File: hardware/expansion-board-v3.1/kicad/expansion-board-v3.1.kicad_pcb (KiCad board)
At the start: 6 copper layers, 100 x 62 mm, 156 parts, among them J1 PinHeader_2x20_P2.54mm_Vertic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, J2 U.FL_Hirose_U.FL-R-SMT-1_Vert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, J4 USB_C_Receptacle_HRO_TYPE-C-3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, J5 U.FL_Hirose_U.FL-R-SMT-1_Vert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, J6 U.FL_Hirose_U.FL-R-SMT-1_Vert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, J8 U.FL_Hirose_U.FL-R-SMT-1_Vert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, Q2 SOT-23, Q3 SOT-23, Q4 SOT-23, Q5 SOT-23, SW1 SolderJumper-2_P1.3mm_Open_Pa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, SW2 SolderJumper-2_P1.3mm_Open_Pa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, U1 SOT-23-5, U10 QFN-48-1EP_7x7mm_P0.5mm_EP5.1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, U11 DFN-8-1EP_2x2mm_P0.5mm_EP0.86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, U12 SOT-363_SC-70-6, U13 AD8319_LFCSP-8-EP, U14 MSOP-8_3x3mm_P0.65mm, U15 SOT-23-6, U16 SOT-363_SC-70-6, U17 SOT-363_SC-70-6, U2 SOT-23-5, U3 SOT-23-5, U4 BNO085_LGA-28, U5 BMP388_LGA-10, U6 LGA-16_3x3mm_P0.5mm, U7 ATGM336H_LCC-18, U8 QFN-56-1EP_7x7mm_P0.4mm_EP3.2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, U9 SOIC-8_5.3x5.3mm_P1.27mm, Y1 Crystal_SMD_3225-4Pin_3.2x2.5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, Y2 Crystal_SMD_3225-4Pin_3.2x2.5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, Y3 Crystal_SMD_3215-2Pin_3.2x1.5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

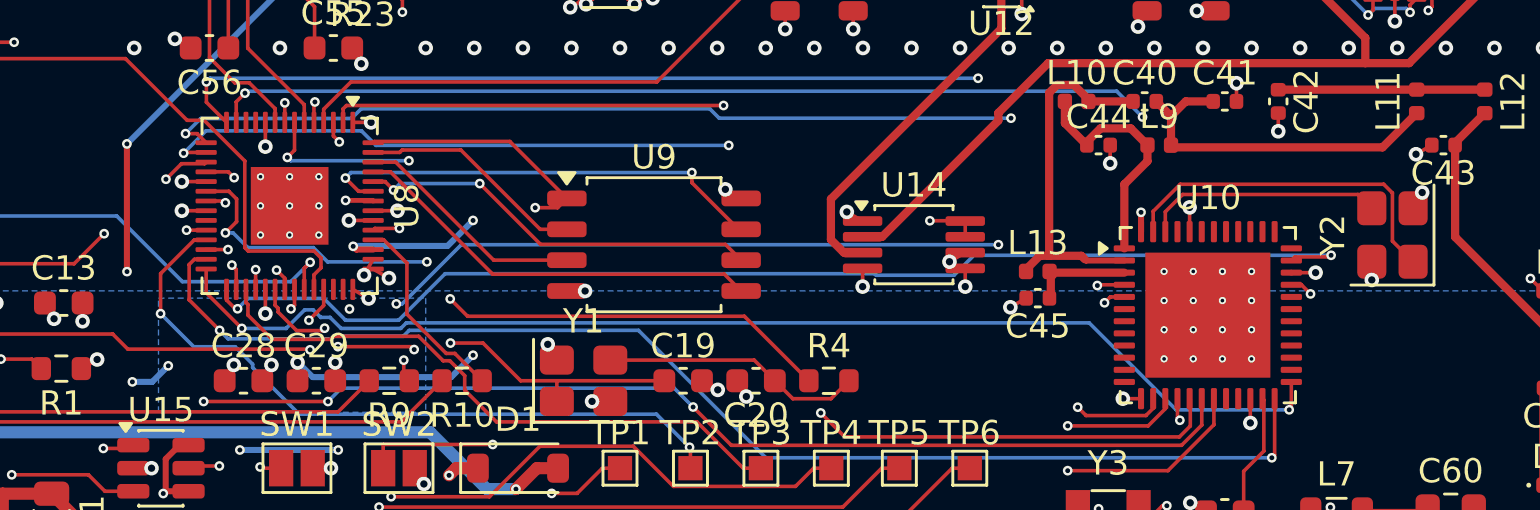
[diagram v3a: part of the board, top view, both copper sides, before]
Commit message: feat(hw): 未连通归零 —— 手工让开两个过孔，两条死线一次布通
    真缺线 0 / 孤立断头铜 0 / 焊盘未接覆铜 0 / 铜层 DRC 0 违例
    射频 160 段全 F.Cu、0 过孔，In1 参考面完整

全项归零，这是 v3.1 第一次。

## 怎么破的

卡了很久的 SUBG_VDDR(U10.45) 和 RP_1V1(U8.23)，我试过 via_keepout 三种形态、
预扇出环、ripup 让路，都不赚（数据在下面）。**评审直接在 KiCad 里把挡路的两个
过孔往外挪了**：

    U8   3V3_DIG 孔  (83.96,80.70)  → (83.35,80.30)
    U8   SWCLK   孔  (84.16,81.50)  → (83.63,82.03)
    U10  3V3_DIG 孔  (125.45,80.56) → (126.58,80.43)

让出通道后他把两条线拉了出来（还顺手在 In2 布通了 SUBG_IRQ 4 段），
剩两个线头交给 route_fix，**一次布通，0 失败**。

## 他先前的两个判断都被数据证实了

**判断一："多个针脚过孔要留下足够空间"** —— 是硬规则，且能算出确切数字：

    通道净空 ≥ 线宽 + 2×净空     信号 0.15+0.30=0.45mm ／ 电源 0.25+0.30=0.55mm

出事的两处正好卡在线下面：U8 两孔之间只有 0.425mm（差 0.125），
U10 pin45 到 3V3_DIG 孔 0.45mm（差 0.10）。差的就是这一点点。

**判断二："先过孔还是先走线"** —— freerouting 是边布线边打孔，先布的线把后面
的孔位堵死。仓里 fanout_ring.py 正是为此写的（文件头："在 freerouting 之前占住
引脚净空环"），但从没进过流程。

## 顺带修掉的、以及试过不赚的

- **route_rf 的缝合过孔写死 0.6/0.3**，而板规是 0.4/0.2。这类孔有 **242 个，
  占全板 451 个过孔的 54%** —— 一大半过孔都胖了 0.1mm 半径。挡住 U8.23 的正是
  其中一个。改到板规后同一对孔的净空 0.325 → 0.425mm。
  **同族问题（改了尺寸，写死的副本没跟着改）这是第 5 次**，前四次见
  memory/project_hardcoded_dimension_copies.md。fanout_v31.py 和 stitch.py 里
  还各有一处，这两个脚本不在流程里，留待启用时修。
- **fanout_ring 排号用错索引**：`row = i % stride` 的 i 是 todo 的序号，而 todo
  滤掉了 GND/RF 引脚，于是和物理位置脱钩——两个只隔 0.4mm 的引脚可能拿到同一排。
  改用该边全部引脚的排序序号。另加 PK_WHY=<ref.pin> 诊断，打印每个候选位被谁挡住。
- **0.4mm pitch 下每脚都扇出物理上不成立**：孔半径 0.2 + stub 半宽 0.075 +
  净空 0.2 = 0.475mm > 引脚间距 0.4mm。所以 72 脚里 25 个"无位"是正常结果。

试过、不赚、已回退的（同一布局，收敛后未连通）：

    什么都不加            2   ← 当时最好
    via_keepout 实心矩形  7   ← 连芯片下方可用区和路过走线的换层都封死
    via_keepout 口字环    3
    预扇出环(先放孔)      5   ← 原理对，但一口气放 47 个孔把空间挤没了
    手工挪 3 个孔     0   ← 精准，代价为零

教训：**这类局部死结，人挪三个孔胜过我改五版算法**。自动化该做的是把规则固化下来
（净空式子、先放孔的顺序、尺寸同步），而不是替代这三下。

## ⚠️ 一个已知风险，下一步必须处理

`gen_pcb.py:194` 是 `pcbnew.NewBoard()` —— **跑 run_route.sh 会从零重建板子，
评审这次手工挪的孔和拉的线全部丢失**。PLACEMENT.py 只固化元件位置，走线没有任何
持久化，而且现在也无法事后识别（全板 IsLocked 都是 False，手画的和 freerouting
布的混在一起）。所以**在补上固化机制之前，不要再跑整条链**。
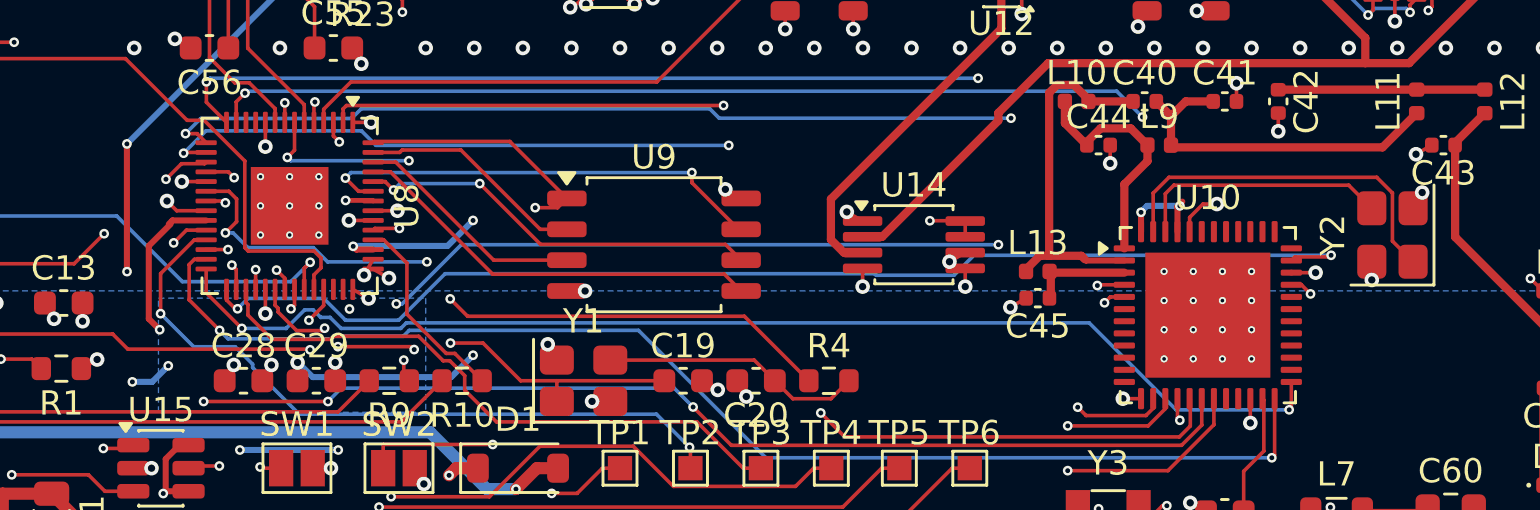
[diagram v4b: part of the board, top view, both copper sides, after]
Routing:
- net RP_1V1: track 39.2 -> 45.7 mm, vias 9 -> 10
- net SUBG_VDDR: track 31.6 -> 34.7 mm, vias 2 -> 3
- net 3V3_DIG: track 36.8 -> 38.5 mm
- net SWCLK: track 41.4 -> 42.9 mm
- net SUBG_X48N: track 9.85 -> 10.6 mm
- net SUBG_X48P: track 14.5 -> 15.2 mm
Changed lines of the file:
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@@
 	)
 	(segment
+		(start 125.45 80.975)
+		(end 125.45 81.5625)
+		(width 0.15)
+		(layer "F.Cu")
+		(net "3V3_DIG")
+	)
+	(segment
 		(start 127.95 88.4375)
 		(end 127.95 89.4375)
@@
 	)
 	(segment
-		(start 63.95 75.975)
-		(end 63.95 76.975)
+		(start 84.9625 80.7)
+		(end 83.75 80.7)
 		(width 0.15)
 		(layer "F.Cu")
@@
 	)
 	(segment
-		(start 84.9625 80.7)
-		(end 83.9625 80.7)
+		(start 63.95 75.975)
+		(end 63.95 76.975)
 		(width 0.15)
 		(layer "F.Cu")
@@
 	)
 	(segment
+		(start 126 80.425)
+		(end 125.45 80.975)
+		(width 0.15)
+		(layer "F.Cu")
+		(net "3V3_DIG")
+	)
+	(segment
 		(start 128.225 97)
 		(end 128.6 96.3505)
@@
 	)
 	(segment
+		(start 126.575 80.425)
+		(end 126 80.425)
+		(width 0.15)
+		(layer "F.Cu")
+		(net "3V3_DIG")
+	)
+	(segment
 		(start 70.225 98.3)
 		(end 69.5755 97.925)
@@
 	)
 	(segment
-		(start 125.45 81.5625)
-		(end 125.45 80.5625)
+		(start 83.75 80.7)
+		(end 83.35 80.3)
 		(width 0.15)
 		(layer "F.Cu")
@@
 	)
 	(via
-		(at 125.45 80.5625)
+		(at 126.575 80.425)
 		(size 0.6)
 		(drill 0.3)
@@
 	)
 	(via
-		(at 83.9625 80.7)
+		(at 83.35 80.3)
 		(size 0.6)
 		(drill 0.3)
@@
 	)
 	(segment
+		(start 124.95 80.525)
+		(end 125.15 80.325)
+		(width 0.25)
+		(layer "F.Cu")
+		(net "SUBG_VDDR")
+	)
+	(segment
 		(start 125.5296 95.7954)
 		(end 124.1228 94.3886)
@@
 	)
 	(segment
+		(start 124.95 81.5625)
+		(end 124.95 80.525)
+		(width 0.25)
+		(layer "F.Cu")
+		(net "SUBG_VDDR")
+	)
+	(segment
 		(start 126.8166 94.5084)
 		(end 131.1541 94.5084)
@@
 		(net "SUBG_VDDR")
 	)
+	(via
+		(at 125.05 80.5)
+		(size 0.4)
+		(drill 0.2)
+		(layers "F.Cu" "B.Cu")
+		(net "SUBG_VDDR")
+	)
+	(segment
+		(start 123.4 80.8)
+		(end 123.7 80.5)
+		(width 0.25)
+		(layer "B.Cu")
+		(net "SUBG_VDDR")
+	)
+	(segment
+		(start 123.7 80.5)
+		(end 125.05 80.5)
+		(width 0.25)
+		(layer "B.Cu")
+		(net "SUBG_VDDR")
+	)
 	(segment
 		(start 123.45 80.7643)
@@
 	)
 	(segment
-		(start 84.8572 82.8758)
-		(end 83.3085 81.3271)
+		(start 84.8572 88.5543)
+		(end 84.8572 83.9572)
 		(width 0.15)
 		(layer "In2.Cu")
@@
 	)
 	(segment
-		(start 83.3085 81.3271)
-		(end 83.3085 79.404)
+		(start 84.8572 83.9572)
+		(end 82.725 81.825)
 		(width 0.15)
 		(layer "In2.Cu")
@@
 	)
 	(segment
-		(start 84.8572 88.5543)
-		(end 84.8572 82.8758)
+		(start 82.725 81.825)
+		(end 82.725 79.9875)
+		(width 0.15)
+		(layer "In2.Cu")
+		(net "SUBG_IRQ")
+	)
+	(segment
+		(start 82.725 79.9875)
+		(end 83.3085 79.404)
 		(width 0.15)
 		(layer "In2.Cu")
@@
 	)
 	(segment
-		(start 124.45 81.5625)
-		(end 124.45 80.744)
+		(start 132 79.65)
+		(end 132.95 80.6)
 		(width 0.15)
 		(layer "F.Cu")
@@
 	)
 	(segment
-		(start 124.45 80.744)
-		(end 125.163 80.031)
+		(start 124.45 81.5625)
+		(end 124.45 80)
 		(width 0.15)
 		(layer "F.Cu")
@@
 	)
 	(segment
-		(start 125.163 80.031)
-		(end 132.381 80.031)
+		(start 124.8 79.65)
+		(end 132 79.65)
 		(width 0.15)
 		(layer "F.Cu")
@@
 	)
 	(segment
-		(start 132.381 80.031)
-		(end 132.95 80.6)
+		(start 124.45 80)
+		(end 124.8 79.65)
 		(width 0.15)
 		(layer "F.Cu")
@@
 	)
 	(segment
-		(start 133.8 79.97)
-		(end 133.8 81.95)
+		(start 124.6 79.325)
+		(end 133.155 79.325)
 		(width 0.15)
 		(layer "F.Cu")
@@
 	)
 	(segment
-		(start 125.0652 79.6108)
-		(end 133.4408 79.6108)
+		(start 133.8 81.95)
+		(end 134.65 82.8)
 		(width 0.15)
 		(layer "F.Cu")
@@
 	)
 	(segment
-		(start 133.8 81.95)
-		(end 134.65 82.8)
+		(start 123.95 81.5625)
+		(end 123.95 79.975)
 		(width 0.15)
 		(layer "F.Cu")
@@
 	)
 	(segment
-		(start 123.95 80.726)
-		(end 125.0652 79.6108)
+		(start 133.155 79.325)
+		(end 133.8 79.97)
 		(width 0.15)
 		(layer "F.Cu")
@@
 	)
 	(segment
-		(start 123.95 81.5625)
-		(end 123.95 80.726)
+		(start 133.8 79.97)
+		(end 133.8 81.95)
 		(width 0.15)
 		(layer "F.Cu")
@@
 	)
 	(segment
-		(start 133.4408 79.6108)
-		(end 133.8 79.97)
+		(start 123.95 79.975)
+		(end 124.6 79.325)
 		(width 0.15)
 		(layer "F.Cu")
@@
 	)
 	(segment
+		(start 82.6 85.15)
+		(end 83.05 85.6)
+		(width 0.25)
+		(layer "F.Cu")
+		(net "RP_1V1")
+	)
+	(segment
 		(start 91.8129 80.2754)
 		(end 91.8375 80.3)
@@
 	)
 	(segment
+		(start 82.6 82.15)
+		(end 82.6 85.15)
+		(width 0.25)
+		(layer "F.Cu")
+		(net "RP_1V1")
+	)
+	(segment
 		(start 85.725 87.7)
 		(end 86.1 87.0505)
@@
 	)
 	(segment
+		(start 84.9625 81.1)
+		(end 83.575 81.1)
+		(width 0.25)
+		(layer "F.Cu")
+		(net "RP_1V1")
+	)
+	(segment
 		(start 91.1493 82.3)
 		(end 91.0149 82.1656)
@@
 	)
 	(segment
+		(start 83.5 81.25)
+		(end 82.6 82.15)
+		(width 0.25)
+		(layer "F.Cu")
+		(net "RP_1V1")
+	)
+	(segment
+		(start 83.575 81.1)
+		(end 83.425 81.25)
+		(width 0.25)
+		(layer "F.Cu")
+		(net "RP_1V1")
+	)
+	(segment
 		(start 90.7031 80.2754)
 		(end 91.8129 80.2754)
@@
 	)
 	(via
+		(at 83.05 85.6)
+		(size 0.4)
+		(drill 0.2)
+		(layers "F.Cu" "B.Cu")
+		(net "RP_1V1")
+	)
+	(via
 		(at 90.4 90.55)
 		(size 0.4)
@@
 	)
 	(segment
-		(start 84.9625 81.5)
-		(end 84.155 81.5)
+		(start 84.15 81.5)
+		(end 83.625 82.025)
 		(width 0.15)
 		(layer "F.Cu")
@@
 	)
 	(segment
+		(start 84.9625 81.5)
+		(end 84.15 81.5)
+		(width 0.15)
+		(layer "F.Cu")
+		(net "SWCLK")
+	)
+	(segment
 		(start 102 91.3)
 		(end 101.2733 91.3)
@@
 	)
 	(via
-		(at 84.155 81.5)
+		(at 83.625 82.025)
 		(size 0.4)
 		(drill 0.2)
@@
 	)
 	(segment
-		(start 84.607 79.2169)
-		(end 84.607 81.048)
+		(start 98.9808 82.104)
+		(end 98.4688 82.616)
 		(width 0.15)
 		(layer "In2.Cu")
@@
 	)
 	(segment
-		(start 93.1712 72.0506)
-		(end 92.8338 72.0506)
+		(start 89.0131 76.1022)
+		(end 89.0131 75.8713)
 		(width 0.15)
 		(layer "In2.Cu")
@@
 	(segment
 		(start 84.607 81.048)
-		(end 84.155 81.5)
+		(end 84.607 79.2169)
 		(width 0.15)
 		(layer "In2.Cu")
@@
 	)
 	(segment
-		(start 89.0131 75.8713)
-		(end 89.0131 76.1022)
+		(start 83.625 82.025)
+		(end 83.63 82.025)
 		(width 0.15)
 		(layer "In2.Cu")
@@
 	)
 	(segment
-		(start 92.8338 72.0506)
-		(end 89.0131 75.8713)
+		(start 84.607 79.2169)
+		(end 86.9745 76.8494)
 		(width 0.15)
 		(layer "In2.Cu")
@@
 	)
 	(segment
-		(start 98.9808 77.8602)
-		(end 93.1712 72.0506)
+		(start 98.4688 91.6198)
+		(end 99.1858 92.3368)
 		(width 0.15)
 		(layer "In2.Cu")
@@
 	(segment
 		(start 98.4688 82.616)
+		(end 98.4688 91.6198)
+		(width 0.15)
+		(layer "In2.Cu")
+		(net "SWCLK")
+	)
+	(segment
+		(start 98.9808 77.8602)
 		(end 98.9808 82.104)
 		(width 0.15)
@@
 	)
 	(segment
-		(start 88.2659 76.8494)
-		(end 86.9745 76.8494)
+		(start 86.9745 76.8494)
+		(end 88.2659 76.8494)
 		(width 0.15)
 		(layer "In2.Cu")
@@
 	)
 	(segment
-		(start 98.4688 91.6198)
-		(end 98.4688 82.616)
+		(start 89.0131 75.8713)
+		(end 92.8338 72.0506)
 		(width 0.15)
 		(layer "In2.Cu")
@@
 	)
 	(segment
-		(start 89.0131 76.1022)
-		(end 88.2659 76.8494)
+		(start 88.2659 76.8494)
+		(end 89.0131 76.1022)
 		(width 0.15)
 		(layer "In2.Cu")
@@
 	)
 	(segment
-		(start 98.9808 82.104)
-		(end 98.9808 77.8602)
+		(start 92.8338 72.0506)
+		(end 93.1712 72.0506)
 		(width 0.15)
 		(layer "In2.Cu")
@@
 	)
 	(segment
-		(start 99.1858 92.3368)
-		(end 98.4688 91.6198)
+		(start 93.1712 72.0506)
+		(end 98.9808 77.8602)
 		(width 0.15)
 		(layer "In2.Cu")
@@
 	)
 	(segment
-		(start 86.9745 76.8494)
-		(end 84.607 79.2169)
+		(start 83.63 82.025)
+		(end 84.607 81.048)
 		(width 0.15)
 		(layer "In2.Cu")
